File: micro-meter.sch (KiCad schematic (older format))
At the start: 129 parts, among them J1 5V_IN, J2 SPI, J3 I2C / UART, J4 IN1, J5 IN2, J6 IN3, J7 IN4, J8 SWD, J9 USB_B_Micro, U1 XC6206P332MR, U2 STM32F411CEU6, U3 MCP6002-ISN, U4 USBLC6-2SC6, Y1 16MHz

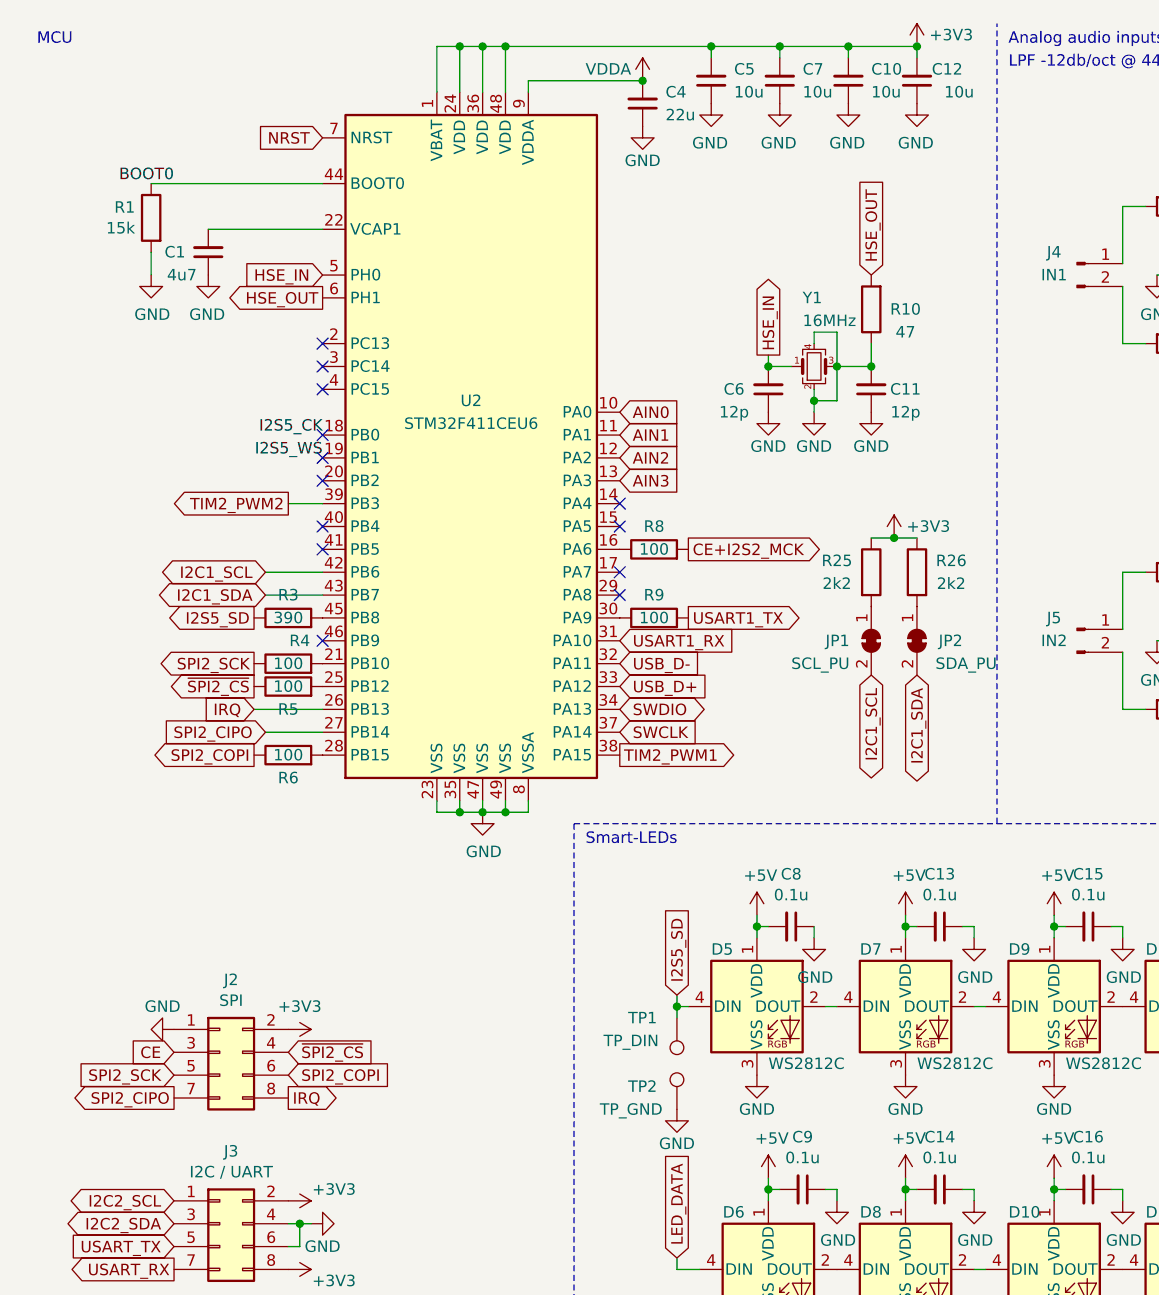
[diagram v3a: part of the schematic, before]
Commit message: Change to 0402 footprints
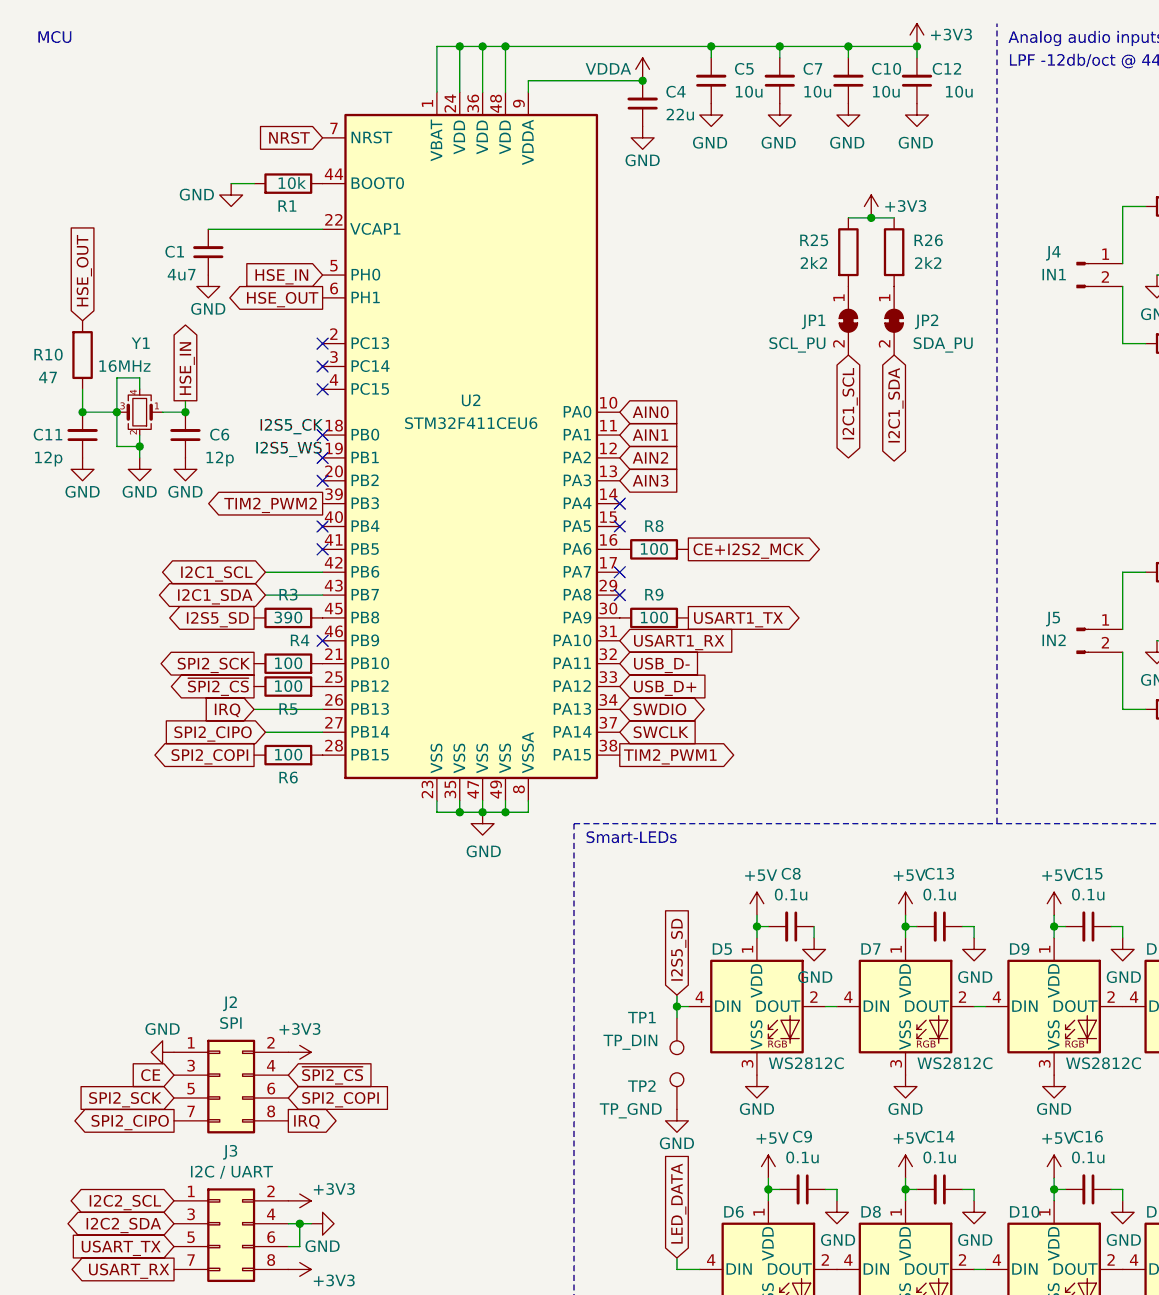
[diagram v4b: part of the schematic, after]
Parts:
- C13, C14, C15, C16, C21, C22, C27, C28, C29, C30, C32, C33, C35, C36, C37, C38, C39, C40, C41, C42, C43, C44, C45, C8, C9: footprint Capacitor_SMD:C_0603_1608Metric -> Capacitor_SMD:C_0402_1005Metric
- FB1, FB2: footprint Resistor_SMD:R_0805_2012Metric -> Inductor_SMD:L_0805_2012Metric
- R1: value 15k -> 10k
- R3, R4, R5, R6, R8, R9: footprint Resistor_SMD:R_0603_1608Metric -> Resistor_SMD:R_0402_1005Metric
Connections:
- net BOOT0: no longer names the net of R1.1, U2.44 (BOOT0)
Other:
- moved on the sheet: C11, C6, J2, JP1, JP2, R1, R10, R25, R26, Y1

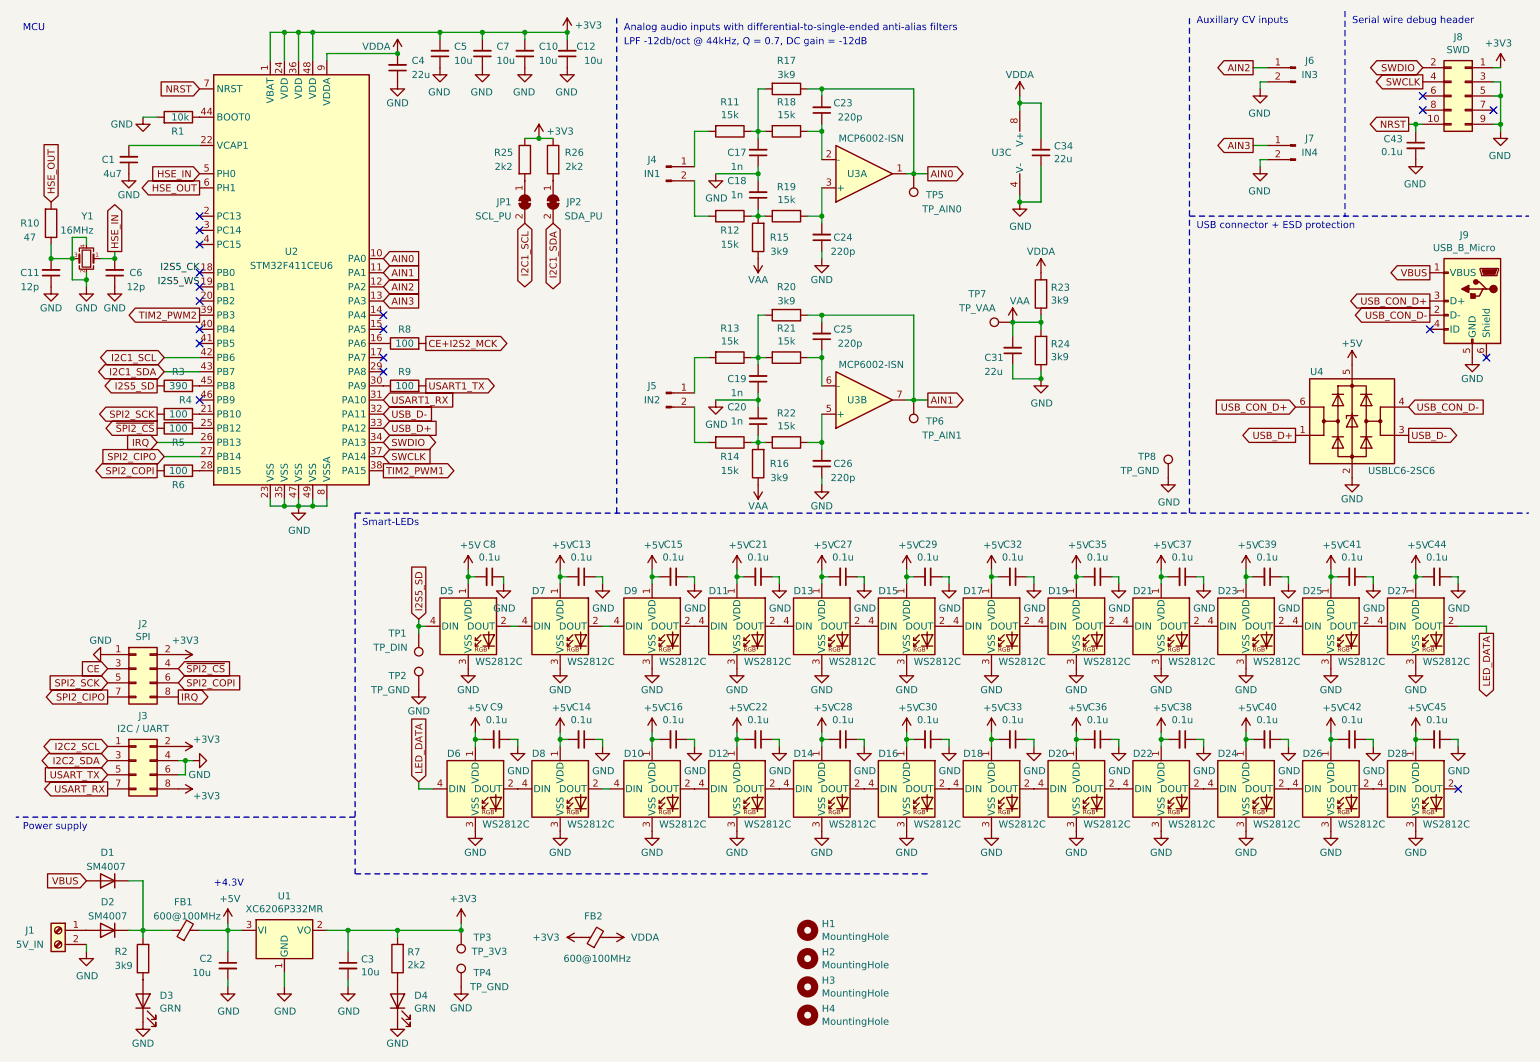
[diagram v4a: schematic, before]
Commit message: Add buck regulator
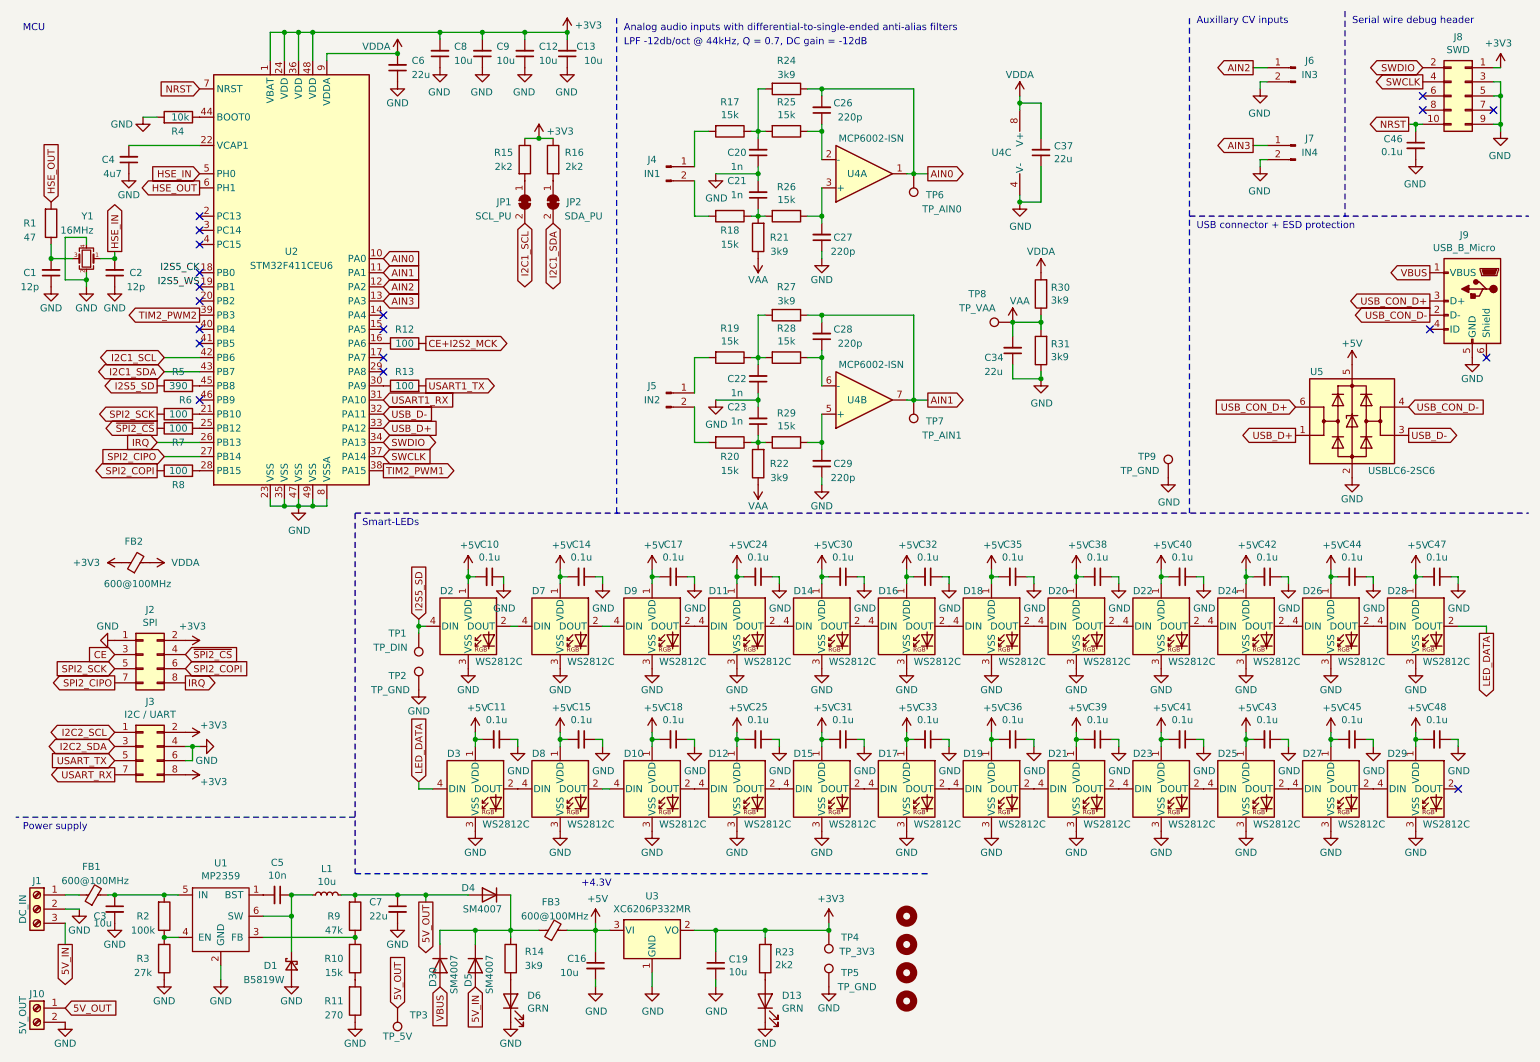
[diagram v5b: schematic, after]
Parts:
- removed J1: 5V_IN, Connector_PinSocket_2.54mm:PinSocket_1x02_P2.54mm_Vertical, symbol Connector:Screw_Terminal_01x02
- added C3: 10u, Capacitor_SMD:C_0805_2012Metric, symbol Device:C_Small
- added C5: 10n, Capacitor_SMD:C_0402_1005Metric, symbol Device:C_Small
- added C7: 22u, Capacitor_SMD:C_0603_1608Metric, symbol Device:C_Small
- added D1: B5819W, Diode_SMD:D_SOD-123, symbol Device:D_Schottky_Small
- added D30: SM4007, Diode_SMD:D_SOD-123F, symbol Diode:SM4007
- added FB1: 600@100MHz, Inductor_SMD:L_0805_2012Metric, symbol Device:Ferrite_Bead_Small
- added J1: DC_IN, Connector_PinSocket_2.54mm:PinSocket_1x03_P2.54mm_Vertical, symbol Connector:Screw_Terminal_01x03
- added J10: 5V_OUT, Connector_PinHeader_2.54mm:PinHeader_1x02_P2.54mm_Vertical, symbol Connector:Screw_Terminal_01x02
- added L1: 10u, Inductor_SMD:L_Sunlord_MWSA0518_5.4x5.2mm, symbol Device:L_Small
- added R10: 15k, Resistor_SMD:R_0402_1005Metric, symbol Device:R
- added R11: 270, Resistor_SMD:R_0402_1005Metric, symbol Device:R
- added R2: 100k, Resistor_SMD:R_0402_1005Metric, symbol Device:R
- added R3: 27k, Resistor_SMD:R_0402_1005Metric, symbol Device:R
- added R9: 47k, Resistor_SMD:R_0402_1005Metric, symbol Device:R
- added TP3: TP_5V, TestPoint:TestPoint_Pad_2.0x2.0mm, symbol Connector:TestPoint
- added U1: MP2359, Package_TO_SOT_SMD:TSOT-23-6, symbol micro-meter:MP2359
- renumbered C11 to C1, C8 to C10, C9 to C11, C10 to C12, C12 to C13, C13 to C14, C14 to C15, C2 to C16, C15 to C17, C16 to C18, C3 to C19, C6 to C2, C17 to C20, C18 to C21, C19 to C22, C20 to C23, C21 to C24, C22 to C25, C23 to C26, C24 to C27, C25 to C28, C26 to C29, C27 to C30, C28 to C31, C29 to C32, C30 to C33, C31 to C34, C32 to C35, C33 to C36, C34 to C37, C35 to C38, C36 to C39, C1 to C4, C37 to C40, C38 to C41, C39 to C42, C40 to C43, C41 to C44, C42 to C45, C43 to C46, C44 to C47, C45 to C48, C4 to C6, C5 to C8, C7 to C9, D4 to D13, D13 to D14, D14 to D15, D15 to D16, D16 to D17, D17 to D18, D18 to D19, D5 to D2, D19 to D20, D20 to D21, D21 to D22, D22 to D23, D23 to D24, D24 to D25, D25 to D26, D26 to D27, D27 to D28, D28 to D29, D6 to D3, D2 to D4, D1 to D5, D3 to D6, FB1 to FB3, R10 to R1, R8 to R12, R9 to R13, R2 to R14, R25 to R15, R26 to R16, R11 to R17, R12 to R18, R13 to R19, R14 to R20, R15 to R21, R16 to R22, R7 to R23, R17 to R24, R18 to R25, R19 to R26, R20 to R27, R21 to R28, R22 to R29, R23 to R30, R24 to R31, R1 to R4, R3 to R5, R4 to R6, R5 to R7, R6 to R8, TP3 to TP4, TP4 to TP5, TP5 to TP6, TP6 to TP7, TP7 to TP8, TP8 to TP9, U1 to U3, U3 to U4, U4 to U5
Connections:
- net GND: now also C3.2, C7.2, D1.2 (A), J1.2 (Pin_2), J10.2 (Pin_2), R11.1, R3.1, U1.2 (GND); no longer C1.2, R1.1, Y1.3
- net VBUS: now also D30.2 (A); no longer D5.2 (A)
- net 5V_OUT: now reaches D4.2 (A)
- net 5V_OUT: now also C7.1, J10.1 (Pin_1), L1.2, R9.2, TP3.1
- net at D4.1 (K), D5.1 (K), FB3.1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: now also D30.1 (K)
- new net: C1.2, R1.1, Y1.3
- new net: C5.2, U1.1 (BST)
- new net: R10.2, R9.1, U1.3 (FB)
- new net: R2.1, R3.2, U1.4 (EN)
- new net: C3.1, FB1.2, R2.2, U1.5 (IN)
- new net: C5.1, D1.1 (K), L1.1, U1.6 (SW)
- new net: FB1.1, J1.1 (Pin_1)
- new net: R10.1, R11.2
- new net 5V_IN: D5.2 (A), J1.3 (Pin_3)
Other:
- moved on the sheet: C16, C19, D13, D4, D5, D6, FB2, FB3, J2, J3, R14, R23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

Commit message: Cleanup schematic
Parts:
- C3: value 10u -> 10uF/25V
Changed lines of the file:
@@
 U 1 1 6006806E
 P 1200 6800
-F 0 "C3" H 1350 6750 50  0000 R CNN
-F 1 "10u" H 1350 6700 50  0000 R CNN
+F 0 "C3" H 1200 7050 50  0000 R CNN
+F 1 "10uF/25V" H 1200 6950 50  0000 R CNN
 F 2 "Capacitor_SMD:C_0805_2012Metric" H 1200 6800 50  0001 C CNN
 F 3 "~" H 1200 6800 50  0001 C CNN
@@
 P 1050 6700
 F 0 "FB1" V 1250 6650 50  0000 L CNN
-F 1 "600@100MHz" V 1150 6450 50  0000 L CNN
+F 1 "600@100MHz" V 1150 6550 50  0000 L CNN
 F 2 "Inductor_SMD:L_0805_2012Metric" V 980 6700 50  0001 C CNN
 F 3 "~" H 1050 6700 50  0001 C CNN
@@
 U 1 1 60681ED2
 P 650 6800
-F 0 "J1" H 650 7000 50  0000 C CNN
+F 0 "J1" H 650 6600 50  0000 C CNN
 F 1 "DC_IN" V 750 6800 50  0000 C CNN
 F 2 "Connector_PinSocket_2.54mm:PinSocket_1x03_P2.54mm_Vertical" H 650 6800 50  0001 C CNN

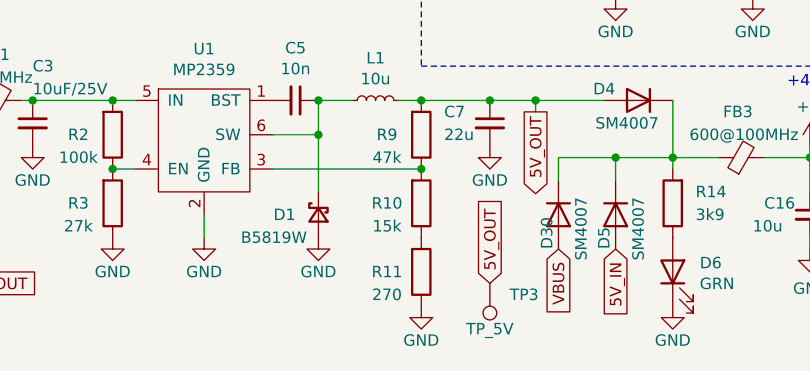
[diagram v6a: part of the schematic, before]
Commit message: Fix buck reg FB values
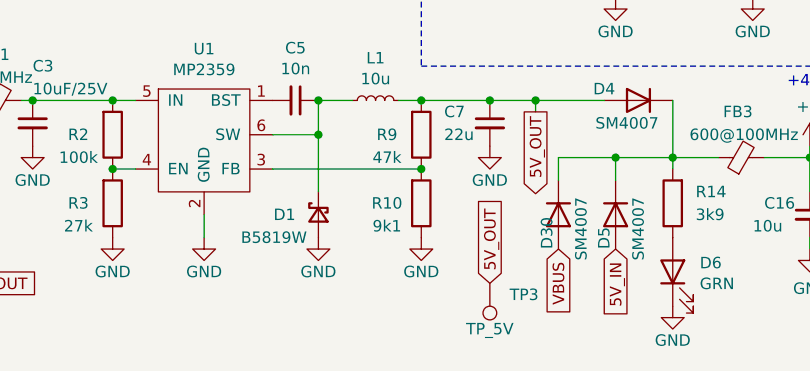
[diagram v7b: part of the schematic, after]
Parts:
- removed R11: 270, Resistor_SMD:R_0402_1005Metric, symbol Device:R
- R10: value 15k -> 9k1; footprint Resistor_SMD:R_0402_1005Metric -> Resistor_SMD:R_0603_1608Metric
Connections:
- net GND: now also R10.1
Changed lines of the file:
@@
 Wire Wire Line
 	850  2350 1000 2350
-$Comp
-L Device:R R11
-U 1 1 6023BAC8
-P 2900 7450
-F 0 "R11" H 2750 7450 50  0000 C CNN
-F 1 "270" H 2750 7550 50  0000 C CNN
-F 2 "Resistor_SMD:R_0402_1005Metric" V 2830 7450 50  0001 C CNN
-F 3 "~" H 2900 7450 50  0001 C CNN
-	1    2900 7450
-	1    0    0    1
-$EndComp
 Connection ~ 2450 6700
 Wire Wire Line
@@
 P 2900 7150
 F 0 "R10" H 2750 7150 50  0000 C CNN
-F 1 "15k" H 2750 7250 50  0000 C CNN
-F 2 "Resistor_SMD:R_0402_1005Metric" V 2830 7150 50  0001 C CNN
+F 1 "9k1" H 2750 7250 50  0000 C CNN
+F 2 "Resistor_SMD:R_0603_1608Metric" V 2830 7150 50  0001 C CNN
 F 3 "~" H 2900 7150 50  0001 C CNN
 	1    2900 7150
@@
 L power:GND #PWR019
 U 1 1 601B9DFA
-P 2900 7600
-F 0 "#PWR019" H 2900 7350 50  0001 C CNN
-F 1 "GND" H 2900 7450 50  0000 C CNN
-F 2 "" H 2900 7600 50  0001 C CNN
-F 3 "" H 2900 7600 50  0001 C CNN
-	1    2900 7600
-	-1   0    0    -1
-$EndComp
+P 2900 7300
+F 0 "#PWR019" H 2900 7050 50  0001 C CNN
+F 1 "GND" H 2900 7150 50  0000 C CNN
+F 2 "" H 2900 7300 50  0001 C CNN
+F 3 "" H 2900 7300 50  0001 C CNN
+	1    2900 7300
+	-1   0    0    -1
+$EndComp
